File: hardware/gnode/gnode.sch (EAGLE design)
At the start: 27 parts, among them U1 ATMEGA328P_TQFP, U3 MCP1700TT, U4 CN3083, U5 HTU21D

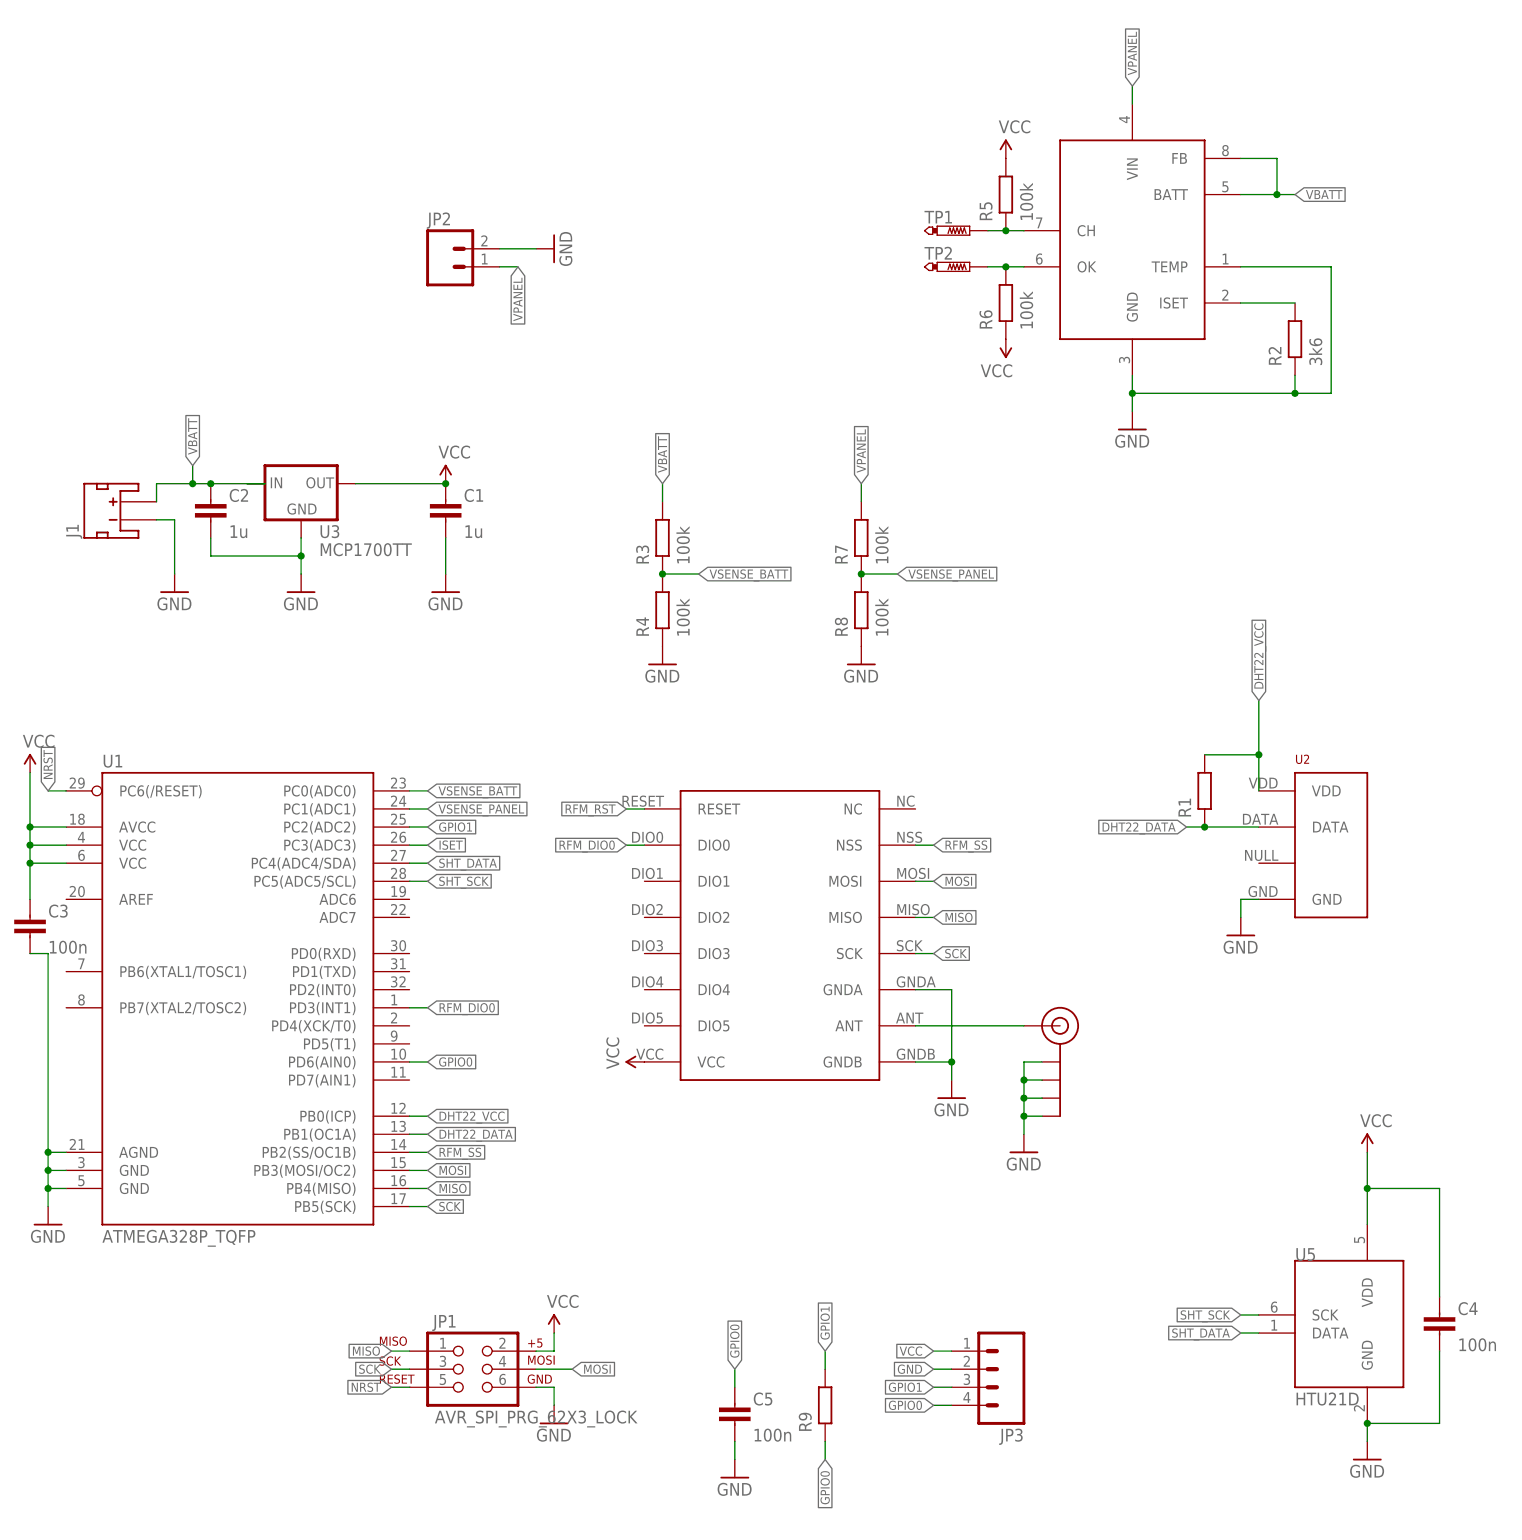
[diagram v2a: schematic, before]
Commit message: uart broken out
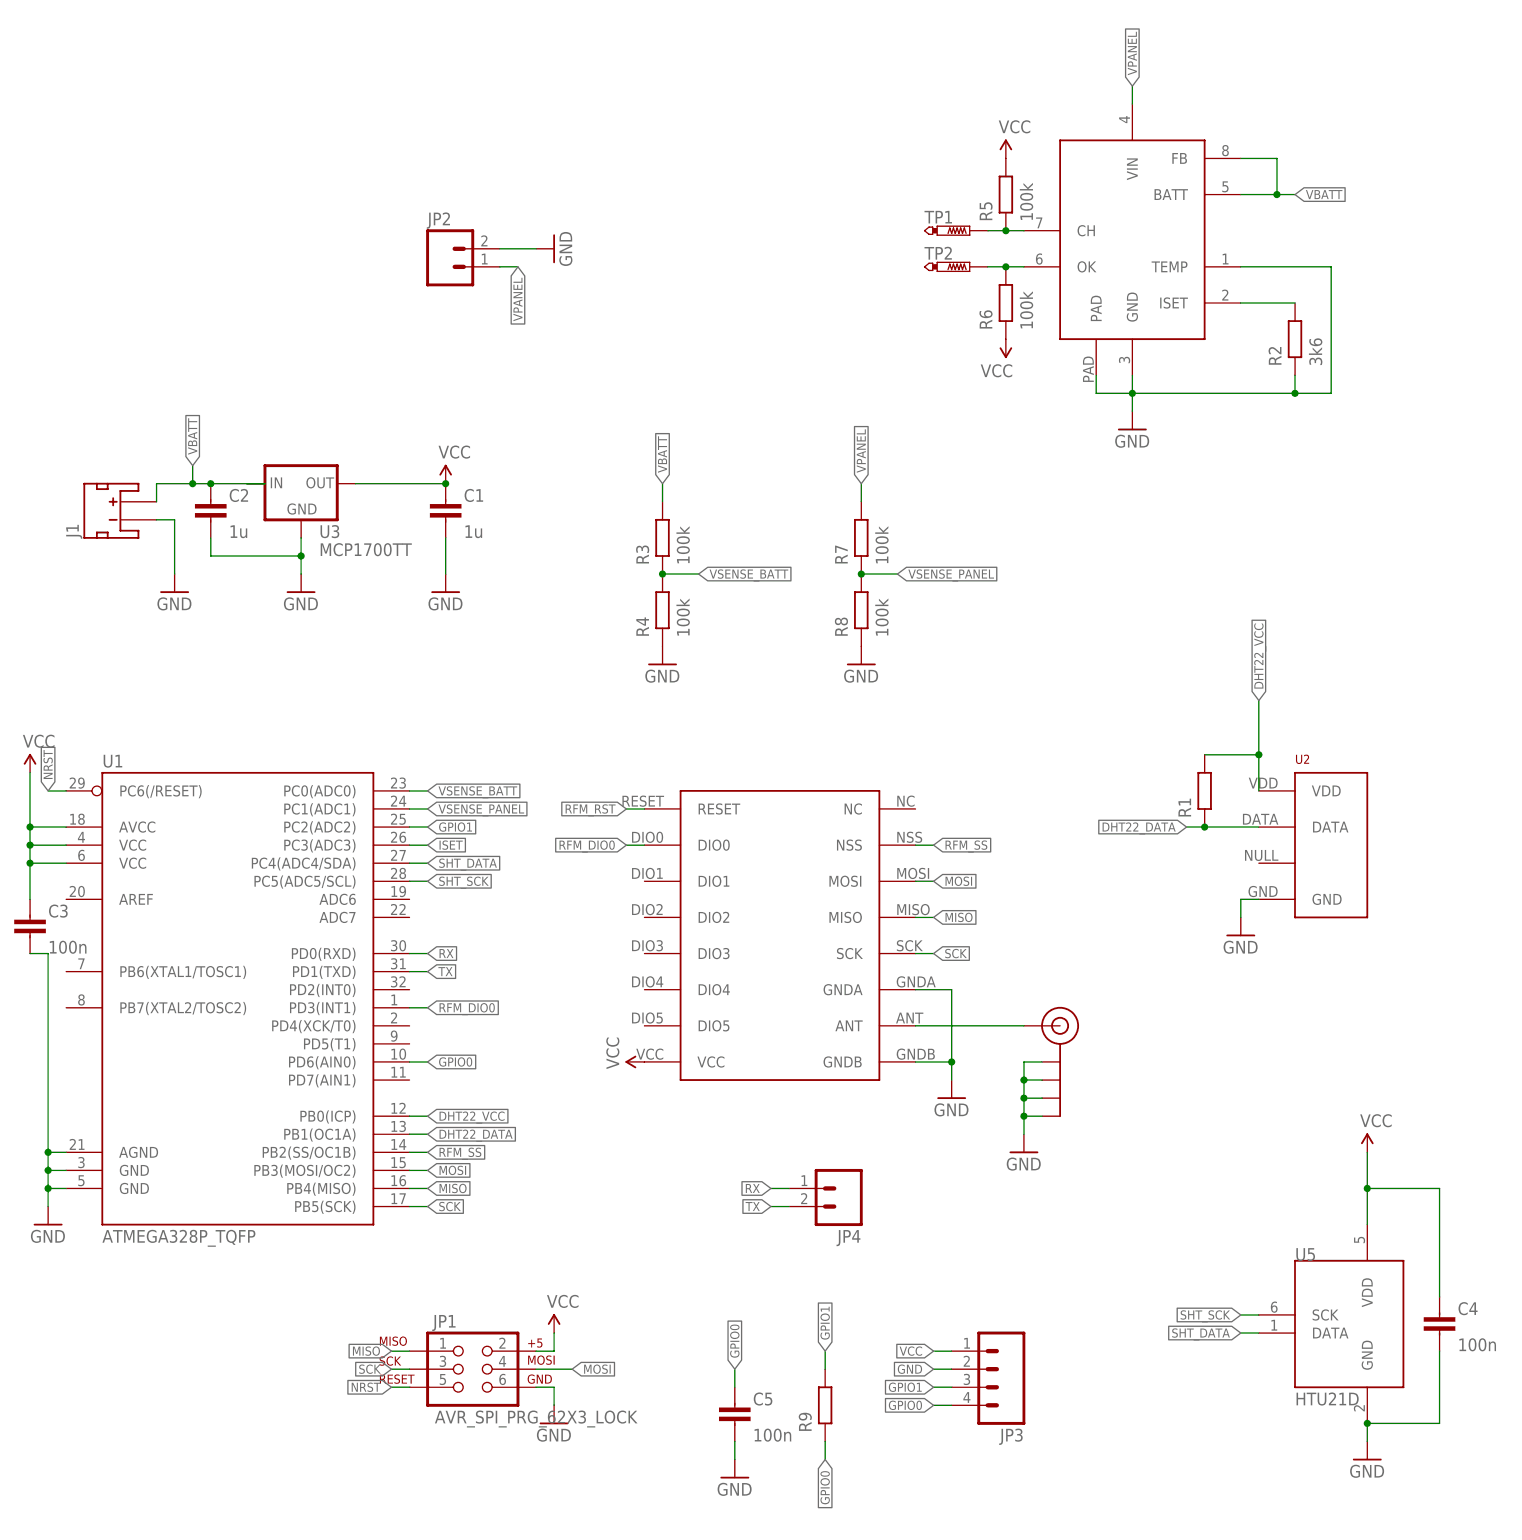
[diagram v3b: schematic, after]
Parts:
- added JP4: (no value), Mine:M02PTH
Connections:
- new net RX: JP4.1, U1.PD0(RXD)
- new net TX: JP4.2, U1.PD1(TXD)
- net GND: now also U4.PAD
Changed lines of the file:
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@@
 <part name="U3" library="dtb" deviceset="MCP1700" device="TT"/>
 <part name="C2" library="passives-7351" deviceset="CAPACITOR" device="0603-N" value="1u"/>
-<part name="U4" library="jonsowman" deviceset="CN3083" device=""/>
 <part name="JP2" library="Mine" deviceset="M02" device="PTH"/>
 <part name="GND10" library="SparkFun-Aesthetics" deviceset="GND" device=""/>
@@
 <part name="C5" library="passives-7351" deviceset="CAPACITOR" device="0603-N" value="100n"/>
 <part name="GND14" library="SparkFun-Aesthetics" deviceset="GND" device=""/>
+<part name="U4" library="jonsowman" deviceset="CN3083" device=""/>
+<part name="JP4" library="Mine" deviceset="M02" device="PTH"/>
 </parts>
 <sheets>
@@
 <instance part="U3" gate="G$1" x="-2.54" y="109.22"/>
 <instance part="C2" gate="G$1" x="-15.24" y="106.68"/>
-<instance part="U4" gate="G$1" x="114.3" y="149.86"/>
 <instance part="JP2" gate="G$1" x="17.78" y="139.7"/>
 <instance part="GND10" gate="1" x="33.02" y="142.24" rot="R90"/>
@@
 </instance>
 <instance part="GND14" gate="1" x="58.42" y="-30.48"/>
+<instance part="U4" gate="G$1" x="114.3" y="149.86"/>
+<instance part="JP4" gate="G$1" x="73.66" y="10.16" rot="R180"/>
 </instances>
 <busses>
@@
 </segment>
 <segment>
-<pinref part="U4" gate="G$1" pin="GND"/>
 <pinref part="GND11" gate="1" pin="GND"/>
 <wire x1="114.3" y1="124.46" x2="114.3" y2="121.92" width="0.1524" layer="91"/>
@@
 <wire x1="137.16" y1="121.92" x2="114.3" y2="121.92" width="0.1524" layer="91"/>
 <junction x="114.3" y="121.92"/>
-<pinref part="U4" gate="G$1" pin="TEMP"/>
 <wire x1="129.54" y1="139.7" x2="142.24" y2="139.7" width="0.1524" layer="91"/>
 <wire x1="142.24" y1="139.7" x2="142.24" y2="121.92" width="0.1524" layer="91"/>
 <wire x1="142.24" y1="121.92" x2="137.16" y2="121.92" width="0.1524" layer="91"/>
 <junction x="137.16" y="121.92"/>
+<pinref part="U4" gate="G$1" pin="GND"/>
+<pinref part="U4" gate="G$1" pin="TEMP"/>
+<pinref part="U4" gate="G$1" pin="PAD"/>
+<wire x1="109.22" y1="124.46" x2="109.22" y2="121.92" width="0.1524" layer="91"/>
+<wire x1="109.22" y1="121.92" x2="114.3" y2="121.92" width="0.1524" layer="91"/>
 </segment>
 <segment>
@@
 </segment>
 <segment>
-<pinref part="U4" gate="G$1" pin="BATT"/>
 <wire x1="129.54" y1="149.86" x2="134.62" y2="149.86" width="0.1524" layer="91"/>
 <label x="137.16" y="149.86" size="1.27" layer="95" xref="yes"/>
-<pinref part="U4" gate="G$1" pin="FB"/>
 <wire x1="134.62" y1="149.86" x2="137.16" y2="149.86" width="0.1524" layer="91"/>
 <wire x1="129.54" y1="154.94" x2="134.62" y2="154.94" width="0.1524" layer="91"/>
 <wire x1="134.62" y1="154.94" x2="134.62" y2="149.86" width="0.1524" layer="91"/>
 <junction x="134.62" y="149.86"/>
+<pinref part="U4" gate="G$1" pin="FB"/>
+<pinref part="U4" gate="G$1" pin="BATT"/>
 </segment>
 <segment>
@@
 <net name="N$2" class="0">
 <segment>
-<pinref part="U4" gate="G$1" pin="CH"/>
 <pinref part="TP1" gate="G$1" pin="TP"/>
 <wire x1="93.98" y1="144.78" x2="96.52" y2="144.78" width="0.1524" layer="91"/>
@@
 <wire x1="96.52" y1="144.78" x2="99.06" y2="144.78" width="0.1524" layer="91"/>
 <junction x="96.52" y="144.78"/>
+<pinref part="U4" gate="G$1" pin="CH"/>
 </segment>
 </net>
 <net name="N$5" class="0">
 <segment>
-<pinref part="U4" gate="G$1" pin="OK"/>
 <pinref part="TP2" gate="G$1" pin="TP"/>
 <wire x1="93.98" y1="139.7" x2="96.52" y2="139.7" width="0.1524" layer="91"/>
@@
 <wire x1="96.52" y1="139.7" x2="99.06" y2="139.7" width="0.1524" layer="91"/>
 <junction x="96.52" y="139.7"/>
+<pinref part="U4" gate="G$1" pin="OK"/>
 </segment>
 </net>
@@
 </segment>
 <segment>
-<pinref part="U4" gate="G$1" pin="VIN"/>
 <wire x1="114.3" y1="162.56" x2="114.3" y2="165.1" width="0.1524" layer="91"/>
 <label x="114.3" y="165.1" size="1.27" layer="95" rot="R90" xref="yes"/>
+<pinref part="U4" gate="G$1" pin="VIN"/>
 </segment>
 <segment>
@@
 </segment>
 <segment>
-<pinref part="U4" gate="G$1" pin="ISET"/>
 <pinref part="R2" gate="G$1" pin="P$2"/>
 <wire x1="129.54" y1="134.62" x2="137.16" y2="134.62" width="0.1524" layer="91"/>
-</segment>
-</net>
+<pinref part="U4" gate="G$1" pin="ISET"/>
+</segment>
+</net>
+<net name="RX" class="0">
+<segment>
+<pinref part="U1" gate="U$1" pin="PD0(RXD)"/>
+<wire x1="12.7" y1="43.18" x2="15.24" y2="43.18" width="0.1524" layer="91"/>
+<label x="15.24" y="43.18" size="1.27" layer="95" xref="yes"/>
+</segment>
+<segment>
+<pinref part="JP4" gate="G$1" pin="1"/>
+<wire x1="66.04" y1="10.16" x2="63.5" y2="10.16" width="0.1524" layer="91"/>
+<label x="63.5" y="10.16" size="1.27" layer="95" rot="R180" xref="yes"/>
+</segment>
+</net>
+<net name="TX" class="0">
+<segment>
+<pinref part="U1" gate="U$1" pin="PD1(TXD)"/>
+<wire x1="12.7" y1="40.64" x2="15.24" y2="40.64" width="0.1524" layer="91"/>
+<label x="15.24" y="40.64" size="1.27" layer="95" xref="yes"/>
+</segment>
+<segment>
+<pinref part="JP4" gate="G$1" pin="2"/>
+<wire x1="66.04" y1="7.62" x2="63.5" y2="7.62" width="0.1524" layer="91"/>
+<label x="63.5" y="7.62" size="1.27" layer="95" rot="R180" xref="yes"/>
+</segment>
+</net>

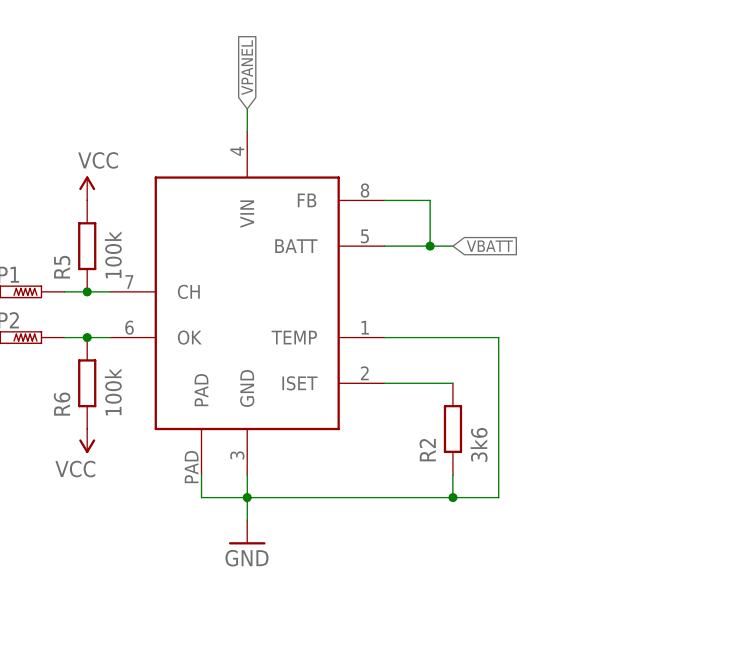
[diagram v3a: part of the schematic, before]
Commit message: added caps for cn3083, oops
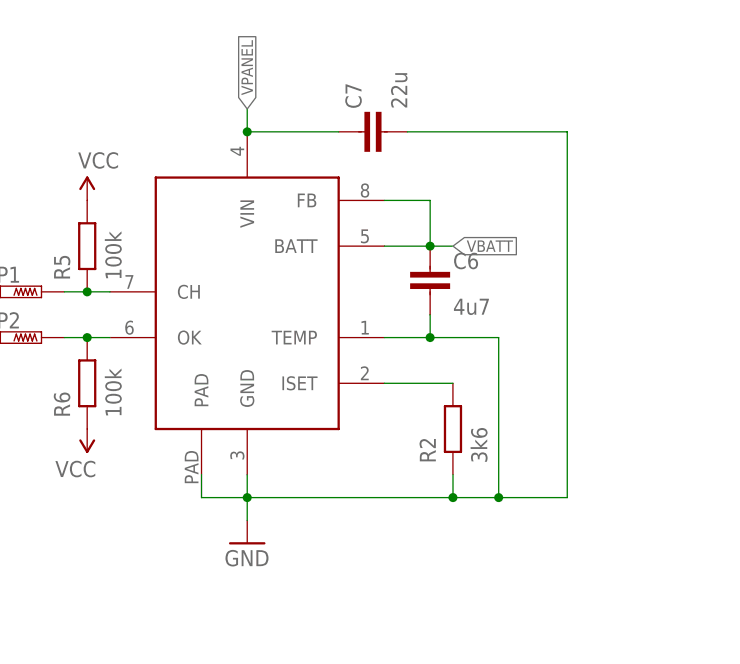
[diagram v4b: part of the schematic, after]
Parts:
- added C6: 4u7, passives-7351:CAPACITOR0603-N
- added C7: 22u, passives-7351:CAPACITOR0603-N
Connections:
- net GND: now also C6.2, C7.2
- net VBATT: now also C6.1
- net VPANEL: now also C7.1
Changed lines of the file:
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@@
 <part name="U4" library="jonsowman" deviceset="CN3083" device=""/>
 <part name="JP4" library="Mine" deviceset="M02" device="PTH"/>
+<part name="C6" library="passives-7351" deviceset="CAPACITOR" device="0603-N" value="4u7"/>
+<part name="C7" library="passives-7351" deviceset="CAPACITOR" device="0603-N" value="22u"/>
 </parts>
 <sheets>
@@
 <instance part="U4" gate="G$1" x="114.3" y="149.86"/>
 <instance part="JP4" gate="G$1" x="73.66" y="10.16" rot="R180"/>
+<instance part="C6" gate="G$1" x="134.62" y="147.32"/>
+<instance part="C7" gate="G$1" x="127" y="162.56" rot="R90"/>
 </instances>
 <busses>
@@
 <wire x1="137.16" y1="121.92" x2="114.3" y2="121.92" width="0.1524" layer="91"/>
 <junction x="114.3" y="121.92"/>
-<wire x1="129.54" y1="139.7" x2="142.24" y2="139.7" width="0.1524" layer="91"/>
+<wire x1="129.54" y1="139.7" x2="134.62" y2="139.7" width="0.1524" layer="91"/>
+<wire x1="134.62" y1="139.7" x2="142.24" y2="139.7" width="0.1524" layer="91"/>
 <wire x1="142.24" y1="139.7" x2="142.24" y2="121.92" width="0.1524" layer="91"/>
 <wire x1="142.24" y1="121.92" x2="137.16" y2="121.92" width="0.1524" layer="91"/>
@@
 <wire x1="109.22" y1="124.46" x2="109.22" y2="121.92" width="0.1524" layer="91"/>
 <wire x1="109.22" y1="121.92" x2="114.3" y2="121.92" width="0.1524" layer="91"/>
+<pinref part="C6" gate="G$1" pin="2"/>
+<wire x1="134.62" y1="142.24" x2="134.62" y2="139.7" width="0.1524" layer="91"/>
+<junction x="134.62" y="139.7"/>
+<pinref part="C7" gate="G$1" pin="2"/>
+<wire x1="132.08" y1="162.56" x2="149.86" y2="162.56" width="0.1524" layer="91"/>
+<wire x1="149.86" y1="162.56" x2="149.86" y2="121.92" width="0.1524" layer="91"/>
+<wire x1="149.86" y1="121.92" x2="142.24" y2="121.92" width="0.1524" layer="91"/>
+<junction x="142.24" y="121.92"/>
 </segment>
 <segment>
@@
 <pinref part="U4" gate="G$1" pin="FB"/>
 <pinref part="U4" gate="G$1" pin="BATT"/>
+<pinref part="C6" gate="G$1" pin="1"/>
 </segment>
 <segment>
@@
 <label x="114.3" y="165.1" size="1.27" layer="95" rot="R90" xref="yes"/>
 <pinref part="U4" gate="G$1" pin="VIN"/>
-</segment>
-<segment>
+<pinref part="C7" gate="G$1" pin="1"/>
+<wire x1="124.46" y1="162.56" x2="114.3" y2="162.56" width="0.1524" layer="91"/>
+<junction x="114.3" y="162.56"/>
+</segment>
+<segment>
